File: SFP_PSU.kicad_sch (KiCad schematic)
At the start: 28 parts

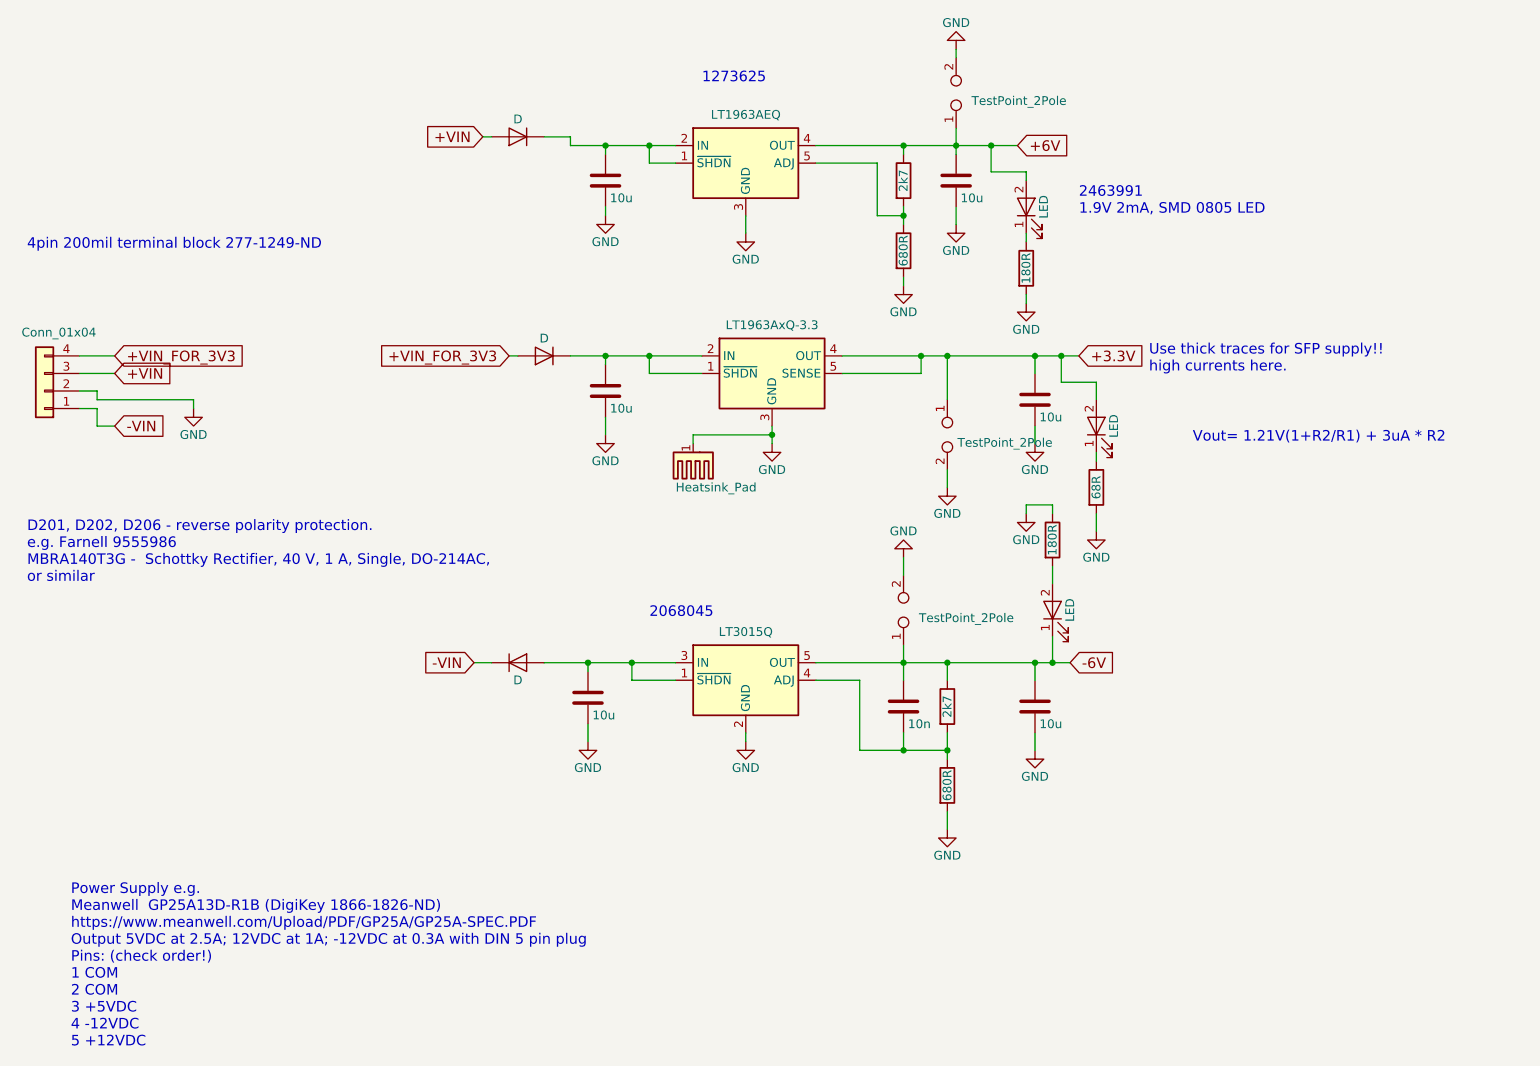
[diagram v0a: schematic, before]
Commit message: update to kicad 9
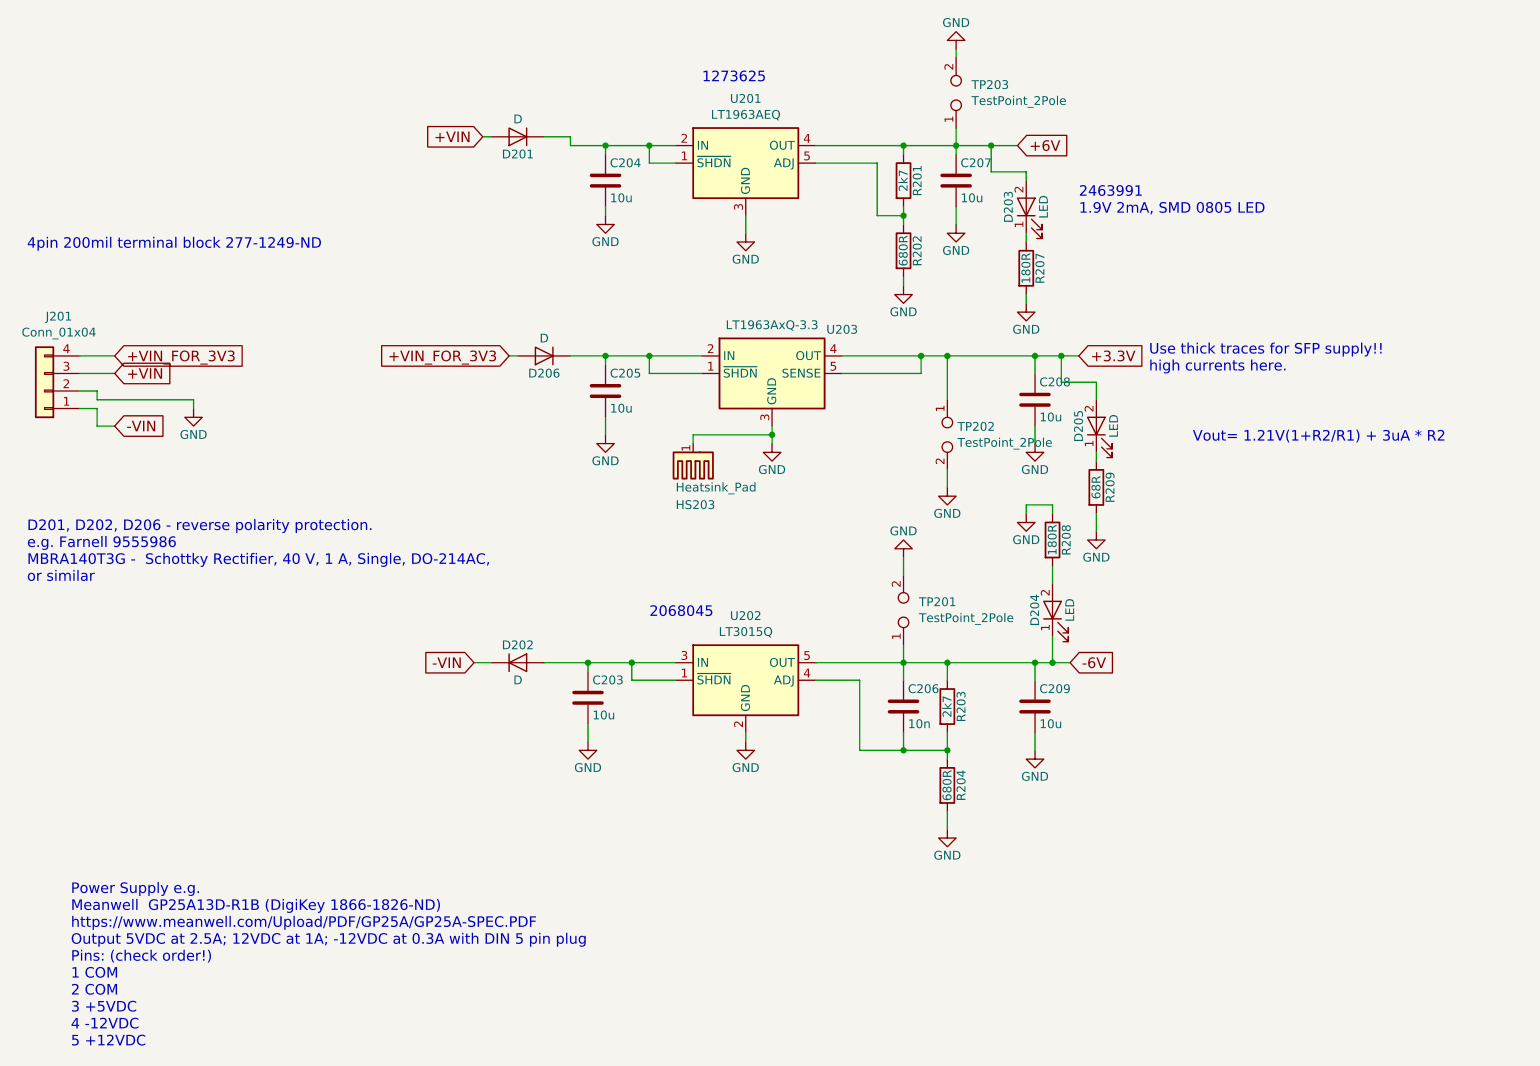
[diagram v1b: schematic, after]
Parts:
- gave numbers to parts that had none: 28
